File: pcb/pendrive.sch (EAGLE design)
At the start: 22 parts, among them IC1 MCP1703CB, U1 F55[0/1]X---RGZ48, U2 MICROSD-MOLEX, X1 USBPCB, Y1 RESONATORSMD

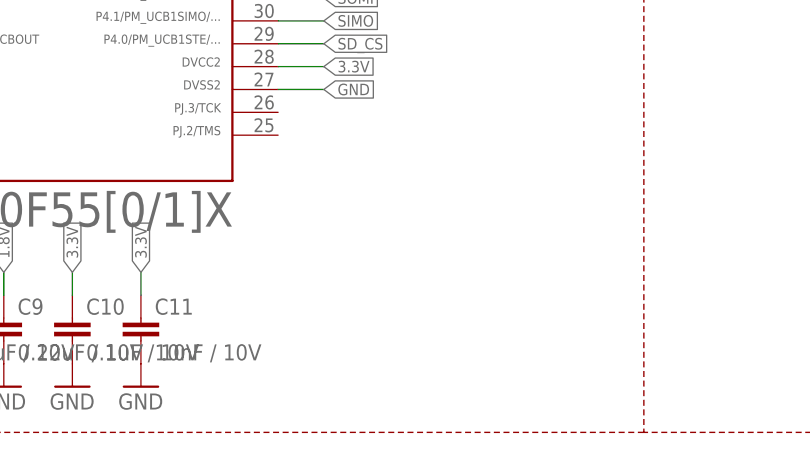
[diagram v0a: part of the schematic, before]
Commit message: Added programming and test points
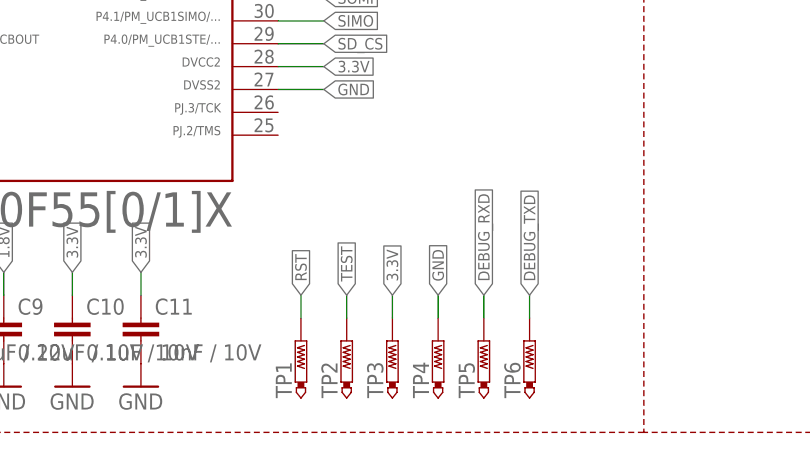
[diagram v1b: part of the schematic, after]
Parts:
- added TP1, TP2, TP3, TP4, TP5, TP6: PTR1TP10SQ, testpad:PTR1TP10SQ
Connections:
- net 3.3V: now also TP3.TP
- net DEBUG_RXD: now also TP5.TP
- net DEBUG_TXD: now also TP6.TP
- net GND: now also TP4.TP
- net RST: now also TP1.TP
- net TEST: now also TP2.TP
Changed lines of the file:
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@@
 <part name="C11" library="SparkFun" deviceset="CAP" device="0402-CAP" value="10nF / 10V"/>
 <part name="GND17" library="SparkFun" deviceset="GND" device=""/>
+<part name="TP1" library="testpad" deviceset="PTR1" device="TP10SQ"/>
+<part name="TP2" library="testpad" deviceset="PTR1" device="TP10SQ"/>
+<part name="TP3" library="testpad" deviceset="PTR1" device="TP10SQ"/>
+<part name="TP4" library="testpad" deviceset="PTR1" device="TP10SQ"/>
+<part name="TP5" library="testpad" deviceset="PTR1" device="TP10SQ"/>
+<part name="TP6" library="testpad" deviceset="PTR1" device="TP10SQ"/>
 </parts>
 <sheets>
@@
 <instance part="C11" gate="G$1" x="55.88" y="10.16"/>
 <instance part="GND17" gate="1" x="55.88" y="5.08"/>
+<instance part="TP1" gate="G$1" x="73.66" y="10.16"/>
+<instance part="TP2" gate="G$1" x="78.74" y="10.16"/>
+<instance part="TP3" gate="G$1" x="83.82" y="10.16"/>
+<instance part="TP4" gate="G$1" x="88.9" y="10.16"/>
+<instance part="TP5" gate="G$1" x="93.98" y="10.16"/>
+<instance part="TP6" gate="G$1" x="99.06" y="10.16"/>
 </instances>
 <busses>
@@
 <pinref part="GND17" gate="1" pin="GND"/>
 </segment>
+<segment>
+<pinref part="TP4" gate="G$1" pin="TP"/>
+<wire x1="88.9" y1="12.7" x2="88.9" y2="15.24" width="0.1524" layer="91"/>
+<label x="88.9" y="15.24" size="1.27" layer="95" rot="R90" xref="yes"/>
+</segment>
 </net>
 <net name="N$4" class="0">
@@
 <label x="55.88" y="17.78" size="1.27" layer="95" rot="R90" xref="yes"/>
 </segment>
+<segment>
+<pinref part="TP3" gate="G$1" pin="TP"/>
+<wire x1="83.82" y1="12.7" x2="83.82" y2="15.24" width="0.1524" layer="91"/>
+<label x="83.82" y="15.24" size="1.27" layer="95" rot="R90" xref="yes"/>
+</segment>
 </net>
 <net name="CLK" class="0">
@@
 <label x="83.82" y="91.44" size="1.27" layer="95" xref="yes"/>
 </segment>
+<segment>
+<pinref part="TP2" gate="G$1" pin="TP"/>
+<wire x1="78.74" y1="12.7" x2="78.74" y2="15.24" width="0.1524" layer="91"/>
+<label x="78.74" y="15.24" size="1.27" layer="95" rot="R90" xref="yes"/>
+</segment>
 </net>
 <net name="RST" class="0">
@@
 <label x="83.82" y="93.98" size="1.27" layer="95" xref="yes"/>
 </segment>
+<segment>
+<pinref part="TP1" gate="G$1" pin="TP"/>
+<wire x1="73.66" y1="12.7" x2="73.66" y2="15.24" width="0.1524" layer="91"/>
+<label x="73.66" y="15.24" size="1.27" layer="95" rot="R90" xref="yes"/>
+</segment>
 </net>
 <net name="1.8V" class="0">
@@
 <label x="76.2" y="55.88" size="1.27" layer="95" xref="yes"/>
 </segment>
+<segment>
+<pinref part="TP5" gate="G$1" pin="TP"/>
+<wire x1="93.98" y1="12.7" x2="93.98" y2="15.24" width="0.1524" layer="91"/>
+<label x="93.98" y="15.24" size="1.27" layer="95" rot="R90" xref="yes"/>
+</segment>
 </net>
 <net name="DEBUG_TXD" class="0">
@@
 <label x="76.2" y="53.34" size="1.27" layer="95" xref="yes"/>
 </segment>
-</net>
+<segment>
+<pinref part="TP6" gate="G$1" pin="TP"/>
+<wire x1="99.06" y1="12.7" x2="99.06" y2="15.24" width="0.1524" layer="91"/>
+<label x="99.06" y="15.24" size="1.27" layer="95" rot="R90" xref="yes"/>
+</segment>
+</net>

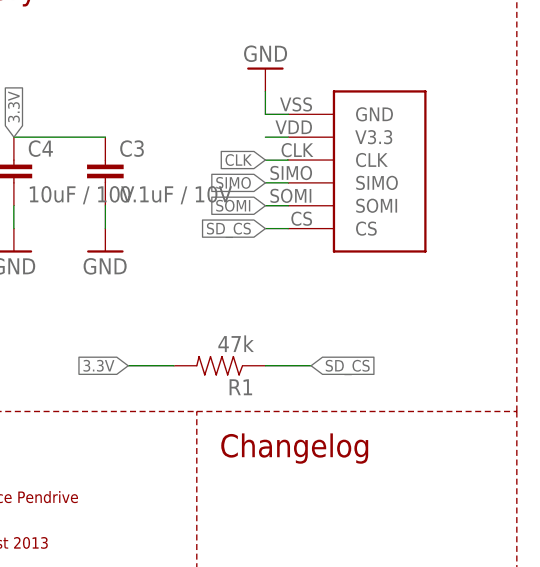
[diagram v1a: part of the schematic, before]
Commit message: Shrinked the board a little bit
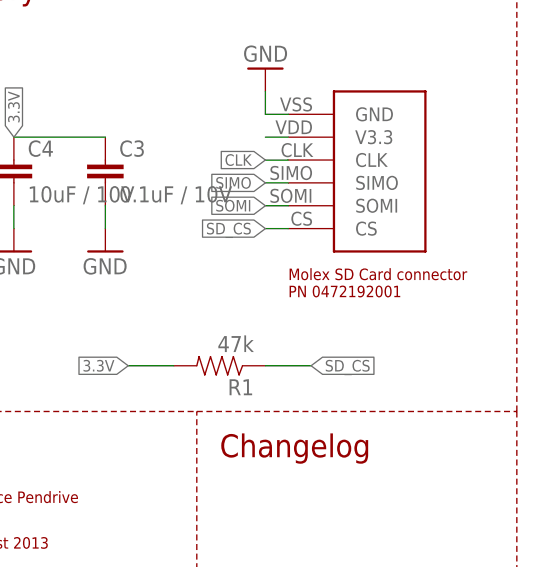
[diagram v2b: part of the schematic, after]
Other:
- note added: "Molex SD Card connector PN 0472192001"
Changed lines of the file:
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@@
 <wire x1="111.76" y1="109.22" x2="111.76" y2="0" width="0.1524" layer="94" style="shortdash"/>
 <text x="114.3" y="104.14" size="2.54" layer="94" font="fixed">USB</text>
+<text x="231.14" y="35.56" size="1.27" layer="94" font="fixed">Molex SD Card connector
+PN 0472192001</text>
 </plain>
 <instances>
@@
 </schematic>
 </drawing>
+<compatibility>
+<note version="6.3" minversion="6.2.2" severity="warning">
+Since Version 6.2.2 text objects can contain more than one line,
+which will not be processed correctly with this version.
+</note>
+</compatibility>
 </eagle>
